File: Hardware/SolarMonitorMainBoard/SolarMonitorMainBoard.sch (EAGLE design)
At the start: 50 parts, among them K1 RT314F12, K2 RT314F12, K3 RT314F12, U1 INA219AIDR, U10 TSR_1-2450, U2 INA219AIDR, U3 INA219AIDR, U4 INA219AIDR, U5 INA219AIDR, U6 INA219AIDR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

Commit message: Cleanup
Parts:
- C1, C2, C3, C4, C5, C6: value (none) -> 0.1uF
- J2: value (none) -> ToTopPrint
- J3: value (none) -> ISP
- R41, R42: value (none) -> 10k
- R7: value (none) -> 100m
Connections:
- net VCC renamed 3V
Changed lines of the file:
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@@
 <part name="SUPPLY4" library="SparkFun-Aesthetics" deviceset="VCC" device=""/>
 <part name="SUPPLY5" library="SparkFun-Aesthetics" deviceset="VCC" device=""/>
-<part name="R41" library="SparkFun-Resistors" deviceset="RESISTOR" device="0805-RES"/>
-<part name="R42" library="SparkFun-Resistors" deviceset="RESISTOR" device="0805-RES"/>
+<part name="R41" library="SparkFun-Resistors" deviceset="RESISTOR" device="0805-RES" value="10k"/>
+<part name="R42" library="SparkFun-Resistors" deviceset="RESISTOR" device="0805-RES" value="10k"/>
 <part name="SUPPLY6" library="SparkFun-Aesthetics" deviceset="VCC" device=""/>
-<part name="C1" library="SparkFun-Capacitors" deviceset="CAP" device="0805"/>
+<part name="C1" library="SparkFun-Capacitors" deviceset="CAP" device="0805" value="0.1uF"/>
 <part name="GND6" library="SparkFun-Aesthetics" deviceset="GND" device=""/>
-<part name="C2" library="SparkFun-Capacitors" deviceset="CAP" device="0805"/>
+<part name="C2" library="SparkFun-Capacitors" deviceset="CAP" device="0805" value="0.1uF"/>
 <part name="GND7" library="SparkFun-Aesthetics" deviceset="GND" device=""/>
-<part name="C3" library="SparkFun-Capacitors" deviceset="CAP" device="0805"/>
+<part name="C3" library="SparkFun-Capacitors" deviceset="CAP" device="0805" value="0.1uF"/>
 <part name="GND8" library="SparkFun-Aesthetics" deviceset="GND" device=""/>
-<part name="C4" library="SparkFun-Capacitors" deviceset="CAP" device="0805"/>
+<part name="C4" library="SparkFun-Capacitors" deviceset="CAP" device="0805" value="0.1uF"/>
 <part name="GND9" library="SparkFun-Aesthetics" deviceset="GND" device=""/>
-<part name="C5" library="SparkFun-Capacitors" deviceset="CAP" device="0805"/>
+<part name="C5" library="SparkFun-Capacitors" deviceset="CAP" device="0805" value="0.1uF"/>
 <part name="GND10" library="SparkFun-Aesthetics" deviceset="GND" device=""/>
 <part name="X1" library="con-phoenix-mkds_5" deviceset="MKDS_5/3-" device="7,62"/>
@@
 <part name="GND16" library="SparkFun-Aesthetics" deviceset="GND" device=""/>
 <part name="SUPPLY10" library="SparkFun-Aesthetics" deviceset="VCC" device=""/>
-<part name="C6" library="SparkFun-Capacitors" deviceset="CAP" device="0805"/>
+<part name="C6" library="SparkFun-Capacitors" deviceset="CAP" device="0805" value="0.1uF"/>
 <part name="GND17" library="SparkFun-Aesthetics" deviceset="GND" device=""/>
 <part name="D2" library="SparkFun-DiscreteSemi" deviceset="DIODE-SCHOTTKY" device="-MBRA140" value="MBRA140"/>
 <part name="D3" library="SparkFun-DiscreteSemi" deviceset="DIODE-SCHOTTKY" device="-MBRA140" value="MBRA140"/>
-<part name="J2" library="SparkFun-Connectors" deviceset="M10X2" device=""/>
+<part name="J2" library="SparkFun-Connectors" deviceset="M10X2" device="" value="ToTopPrint"/>
 <part name="GND12" library="SparkFun-Aesthetics" deviceset="GND" device=""/>
 <part name="SUPPLY11" library="SparkFun-Aesthetics" deviceset="VCC" device=""/>
@@
 <part name="GND18" library="SparkFun-Aesthetics" deviceset="GND" device=""/>
 <part name="GND19" library="SparkFun-Aesthetics" deviceset="GND" device=""/>
-<part name="R7" library="SparkFun-Resistors" deviceset="RESISTOR" device="2512"/>
+<part name="R7" library="SparkFun-Resistors" deviceset="RESISTOR" device="2512" value="100m"/>
 <part name="U7" library="SparkFun-DigitalIC" deviceset="ATMEGA328P_TQFP" device="" value="ATMEGA328P_TQFP"/>
 <part name="GND15" library="SparkFun-Aesthetics" deviceset="GND" device=""/>
@@
 <part name="GND25" library="SparkFun-Aesthetics" deviceset="GND" device=""/>
 <part name="X5" library="con-phoenix-mkds_5" deviceset="MKDS_5/3-" device="7,62"/>
-<part name="J3" library="SparkFun-Connectors" deviceset="M04X2" device=""/>
+<part name="J3" library="SparkFun-Connectors" deviceset="M04X2" device="" value="ISP"/>
 <part name="C8" library="SparkFun-Capacitors" deviceset="CAP" device="0805" value="0.1uF"/>
 <part name="D21" library="SparkFun-DiscreteSemi" deviceset="DIODE-ZENER" device="3.3V" value="3.3V"/>
@@
 </segment>
 </net>
-<net name="VCC" class="0">
+<net name="3V" class="0">
 <segment>
 <pinref part="SUPPLY1" gate="G$1" pin="VCC"/>

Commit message: Replace BAT schottky with SMA part.
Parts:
- D1: value RB751 -> B340A; device SparkFun-DiscreteSemi:DIODE-SCHOTTKY-RB751 -> SparkFun-DiscreteSemi:DIODE-SCHOTTKY-B340A
- R11, R12, R13: value (none) -> 15k
- R21, R22, R23: value (none) -> 5.1k
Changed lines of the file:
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@@
 <part name="GND14" library="SparkFun-Aesthetics" deviceset="GND" device=""/>
 <part name="SUPPLY8" library="SparkFun-Aesthetics" deviceset="VCC" device=""/>
-<part name="D1" library="SparkFun-DiscreteSemi" deviceset="DIODE-SCHOTTKY" device="-RB751" value="RB751"/>
+<part name="D1" library="SparkFun-DiscreteSemi" deviceset="DIODE-SCHOTTKY" device="-B340A" value="B340A"/>
 <part name="R1" library="resistor-shunt" deviceset="SMV" device="" value="5m"/>
 <part name="R2" library="resistor-shunt" deviceset="SMV" device="" value="5m"/>
@@
 <part name="GND21" library="SparkFun-Aesthetics" deviceset="GND" device=""/>
 <part name="X6" library="con-phoenix-508" deviceset="MKDSN1,5/8-5,08" device=""/>
-<part name="R11" library="SparkFun-Resistors" deviceset="RESISTOR" device="0805-RES"/>
-<part name="R21" library="SparkFun-Resistors" deviceset="RESISTOR" device="0805-RES"/>
+<part name="R11" library="SparkFun-Resistors" deviceset="RESISTOR" device="0805-RES" value="15k"/>
+<part name="R21" library="SparkFun-Resistors" deviceset="RESISTOR" device="0805-RES" value="5.1k"/>
 <part name="GND22" library="SparkFun-Aesthetics" deviceset="GND" device=""/>
 <part name="GND23" library="SparkFun-Aesthetics" deviceset="GND" device=""/>
 <part name="K1" library="relay" deviceset="RT?F*" device="314" technology="12"/>
-<part name="R12" library="SparkFun-Resistors" deviceset="RESISTOR" device="0805-RES"/>
-<part name="R22" library="SparkFun-Resistors" deviceset="RESISTOR" device="0805-RES"/>
+<part name="R12" library="SparkFun-Resistors" deviceset="RESISTOR" device="0805-RES" value="15k"/>
+<part name="R22" library="SparkFun-Resistors" deviceset="RESISTOR" device="0805-RES" value="5.1k"/>
 <part name="GND24" library="SparkFun-Aesthetics" deviceset="GND" device=""/>
-<part name="R13" library="SparkFun-Resistors" deviceset="RESISTOR" device="0805-RES"/>
-<part name="R23" library="SparkFun-Resistors" deviceset="RESISTOR" device="0805-RES"/>
+<part name="R13" library="SparkFun-Resistors" deviceset="RESISTOR" device="0805-RES" value="15k"/>
+<part name="R23" library="SparkFun-Resistors" deviceset="RESISTOR" device="0805-RES" value="5.1k"/>
 <part name="GND25" library="SparkFun-Aesthetics" deviceset="GND" device=""/>
 <part name="X5" library="con-phoenix-mkds_5" deviceset="MKDS_5/3-" device="7,62"/>

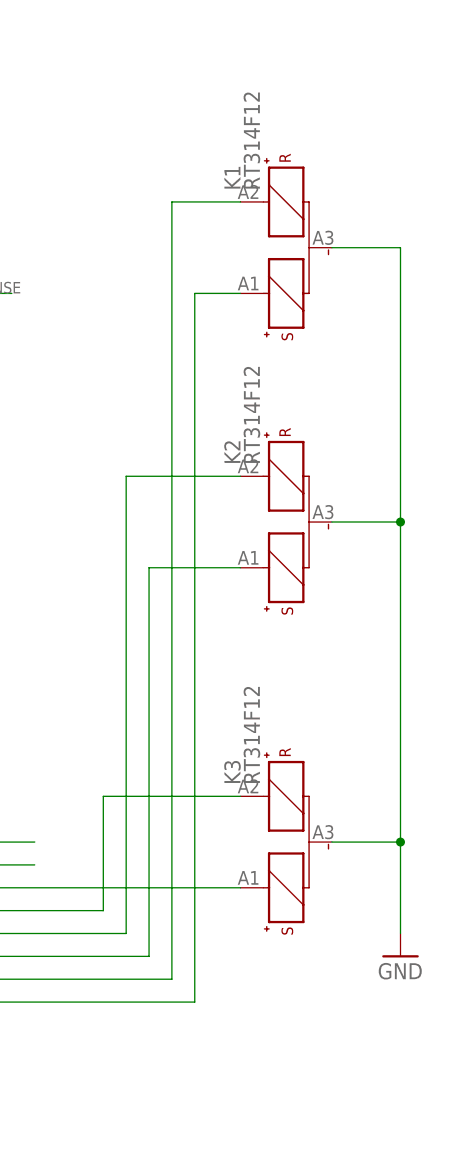
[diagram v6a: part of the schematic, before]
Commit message: Fix ground instead of +12V error in schematic routing on board not done yet.
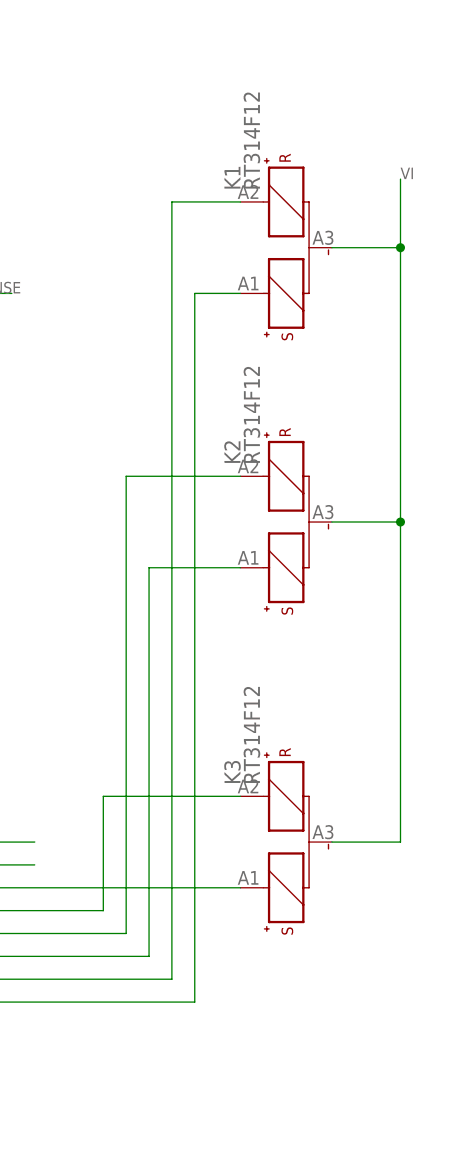
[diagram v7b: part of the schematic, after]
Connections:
- net GND: no longer K11.-, K21.-, K31.-
- net VI: now also K11.-, K21.-, K31.-
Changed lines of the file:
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@@
 <part name="U8" library="Texas Instruments_By_element14_Batch_1" deviceset="ULN2803ADW" device=""/>
 <part name="GND18" library="SparkFun-Aesthetics" deviceset="GND" device=""/>
-<part name="GND19" library="SparkFun-Aesthetics" deviceset="GND" device=""/>
 <part name="R7" library="SparkFun-Resistors" deviceset="RESISTOR" device="2512" value="100m"/>
 <part name="U7" library="SparkFun-DigitalIC" deviceset="ATMEGA328P_TQFP" device="" value="ATMEGA328P_TQFP"/>
@@
 <instance part="U8" gate="A" x="292.1" y="314.96"/>
 <instance part="GND18" gate="1" x="269.24" y="292.1"/>
-<instance part="GND19" gate="1" x="370.84" y="309.88"/>
 <instance part="R7" gate="G$1" x="-53.34" y="152.4" rot="R90"/>
 <instance part="U7" gate="U$1" x="203.2" y="314.96"/>
@@
 </segment>
 <segment>
-<pinref part="GND19" gate="1" pin="GND"/>
-<wire x1="370.84" y1="312.42" x2="370.84" y2="322.58" width="0.1524" layer="91"/>
-<pinref part="K3" gate="1" pin="-"/>
-<wire x1="370.84" y1="322.58" x2="363.22" y2="322.58" width="0.1524" layer="91"/>
-<wire x1="370.84" y1="322.58" x2="370.84" y2="358.14" width="0.1524" layer="91"/>
-<junction x="370.84" y="322.58"/>
-<pinref part="K2" gate="1" pin="-"/>
-<wire x1="370.84" y1="358.14" x2="363.22" y2="358.14" width="0.1524" layer="91"/>
-<pinref part="K1" gate="1" pin="-"/>
-<wire x1="363.22" y1="388.62" x2="370.84" y2="388.62" width="0.1524" layer="91"/>
-<wire x1="370.84" y1="388.62" x2="370.84" y2="358.14" width="0.1524" layer="91"/>
-<junction x="370.84" y="358.14"/>
-</segment>
-<segment>
 <pinref part="C6" gate="G$1" pin="1"/>
 <pinref part="GND17" gate="1" pin="GND"/>
@@
 <label x="314.96" y="299.72" size="1.27" layer="95"/>
 </segment>
-</net>
+<segment>
+<pinref part="K3" gate="1" pin="-"/>
+<wire x1="370.84" y1="322.58" x2="363.22" y2="322.58" width="0.1524" layer="91"/>
+<wire x1="370.84" y1="322.58" x2="370.84" y2="358.14" width="0.1524" layer="91"/>
+<pinref part="K2" gate="1" pin="-"/>
+<wire x1="370.84" y1="358.14" x2="363.22" y2="358.14" width="0.1524" layer="91"/>
+<pinref part="K1" gate="1" pin="-"/>
+<wire x1="363.22" y1="388.62" x2="370.84" y2="388.62" width="0.1524" layer="91"/>
+<wire x1="370.84" y1="388.62" x2="370.84" y2="358.14" width="0.1524" layer="91"/>
+<junction x="370.84" y="358.14"/>
+<wire x1="370.84" y1="396.24" x2="370.84" y2="388.62" width="0.1524" layer="91"/>
+<junction x="370.84" y="388.62"/>
+<label x="370.84" y="396.24" size="1.27" layer="95"/>
+</segment>
+</net>
